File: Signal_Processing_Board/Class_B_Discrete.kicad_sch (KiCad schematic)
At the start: 29 parts, among them Q2 Q_amp-c-1, Q3 Q_amp-c-2, Q4 Q_amp-c-3, Q5 Q_amp-c-4, U11 U_amp-c_1, U12 U_amp-c_2

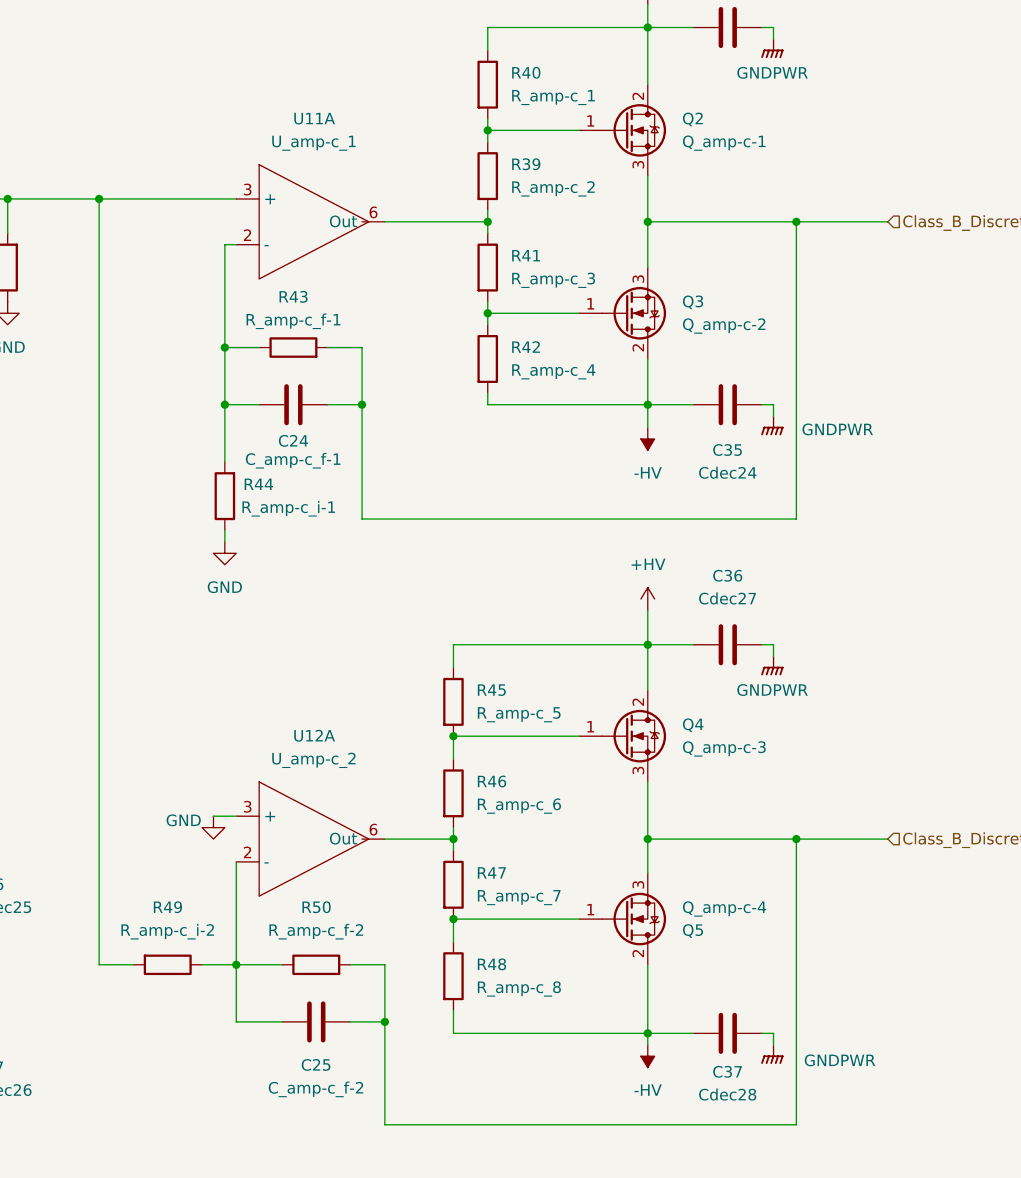
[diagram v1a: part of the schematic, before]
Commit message: First ordered version of Board
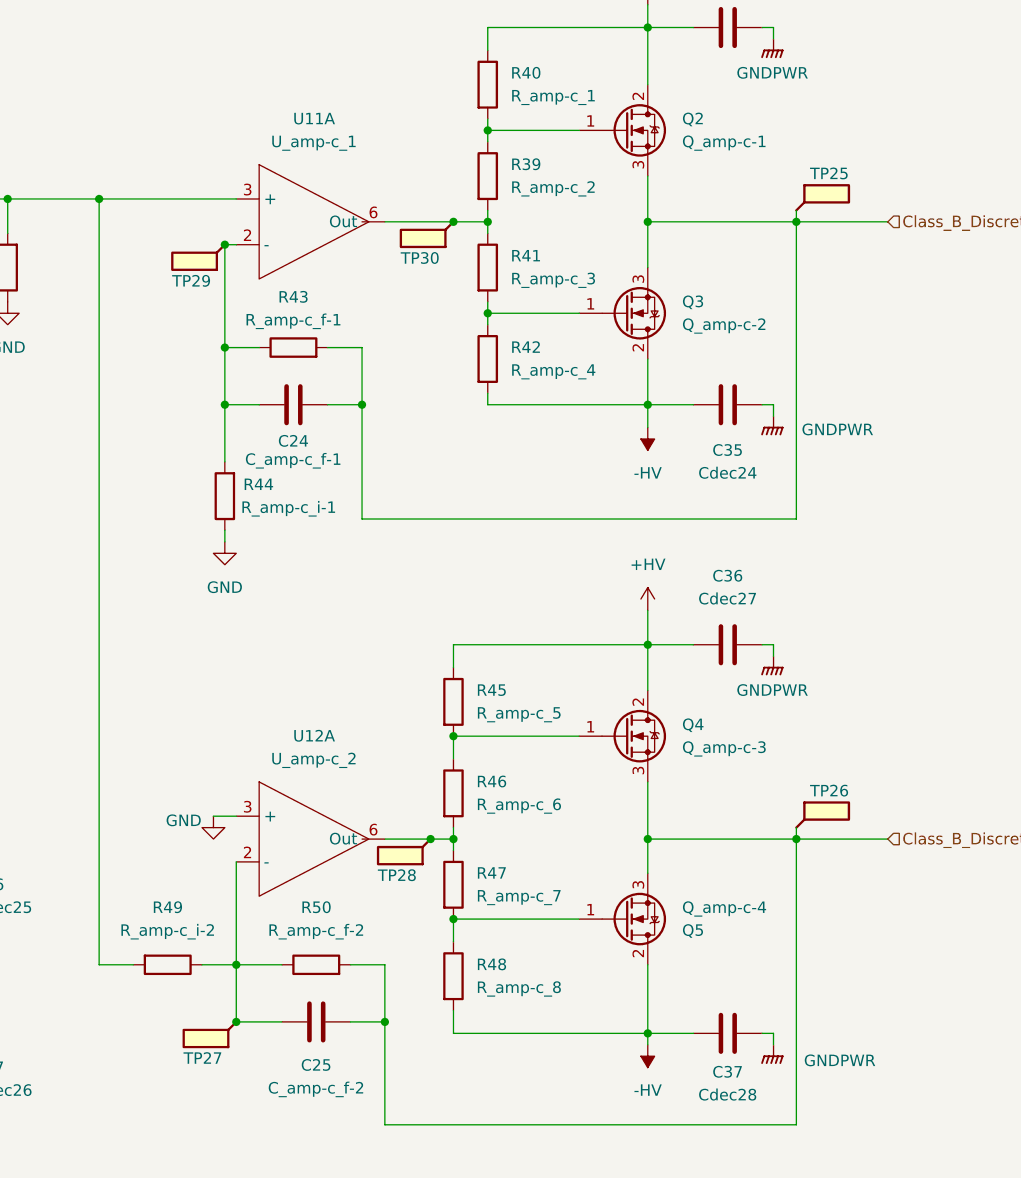
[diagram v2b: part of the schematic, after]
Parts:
- added TP25, TP26, TP27, TP28, TP29, TP30: TestPoint_Flag, TestPoint:TestPoint_Pad_D1.5mm, symbol Connector:TestPoint_Flag
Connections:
- net Class_B_Discrete_Out_+: now also TP25.1
- net Class_B_Discrete_Out_-: now also TP26.1
- net at R39.2, R41.1, U11.6 (Out): now also TP30.1
- net at C25.1, R49.1, R50.1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: now also TP27.1
- net at C24.1, R43.1, R44.2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: now also TP29.1
- net at R46.2, R47.1, U12.6 (Out): now also TP28.1

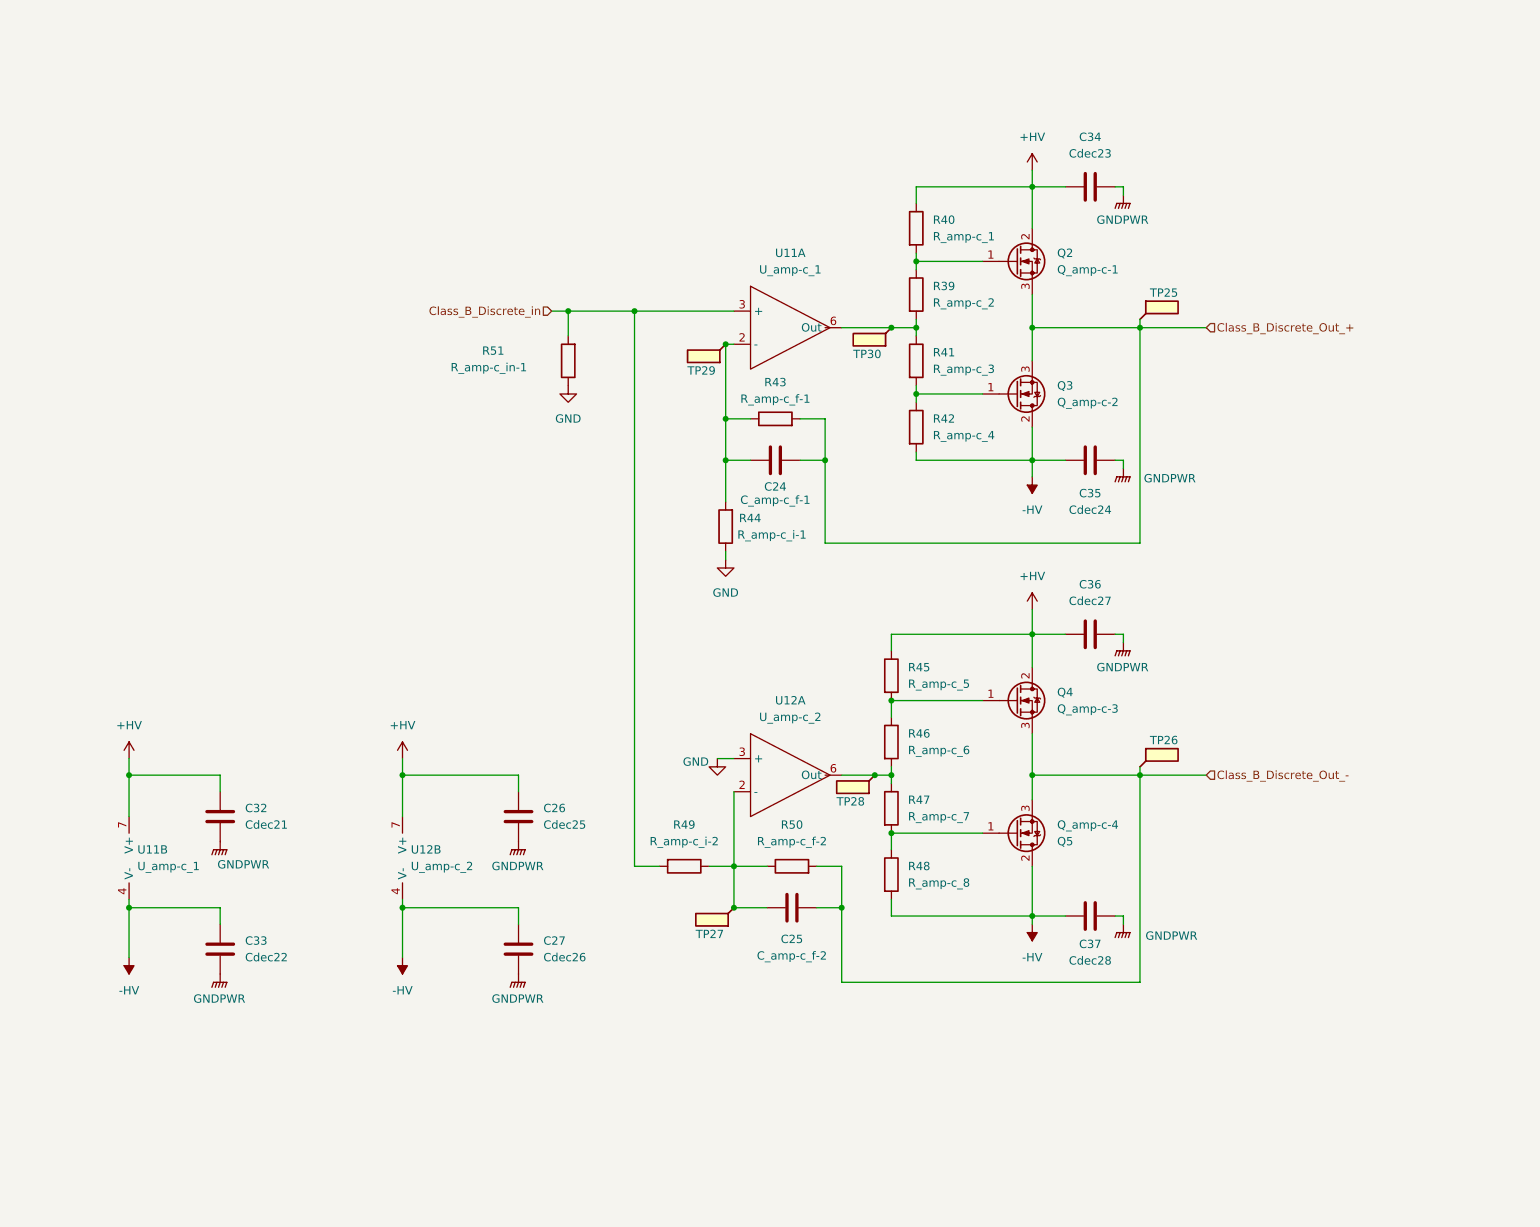
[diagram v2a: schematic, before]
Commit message: Final version of the board, updated with lessons from first version
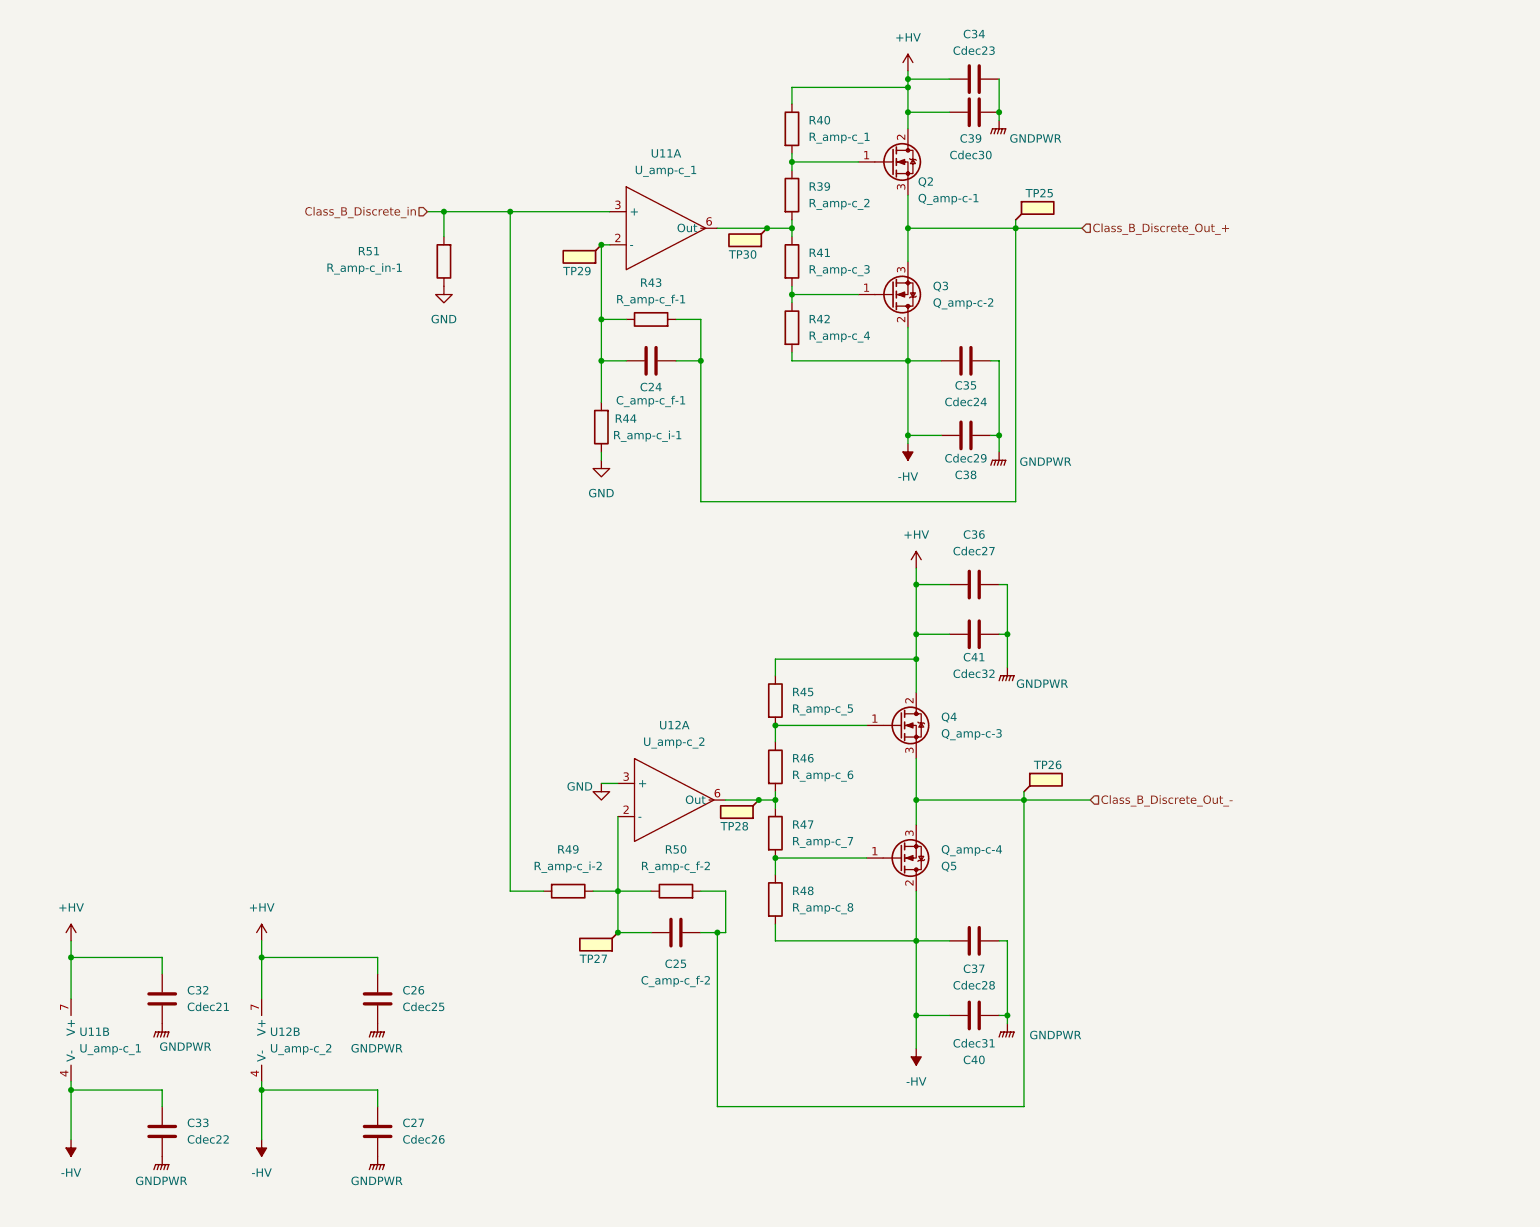
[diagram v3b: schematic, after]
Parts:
- added C38: Cdec29, Capacitor_THT:CP_Radial_D10.0mm_P5.00mm, symbol Device:C
- added C39: Cdec30, Capacitor_THT:CP_Radial_D10.0mm_P5.00mm, symbol Device:C
- added C40: Cdec31, Capacitor_THT:CP_Radial_D10.0mm_P5.00mm, symbol Device:C
- added C41: Cdec32, Capacitor_THT:CP_Radial_D10.0mm_P5.00mm, symbol Device:C
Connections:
- net +HV: now also C39.1, C41.1
- net -HV: now also C38.2, C40.2
- net GNDPWR: now also C38.1, C39.2, C40.1, C41.2
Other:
- moved on the sheet: C24, C25, C26, C27, C32, C33, C34, C35, C36, C37, Q2, Q3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

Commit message: Updated file structure and added PDF of schematic
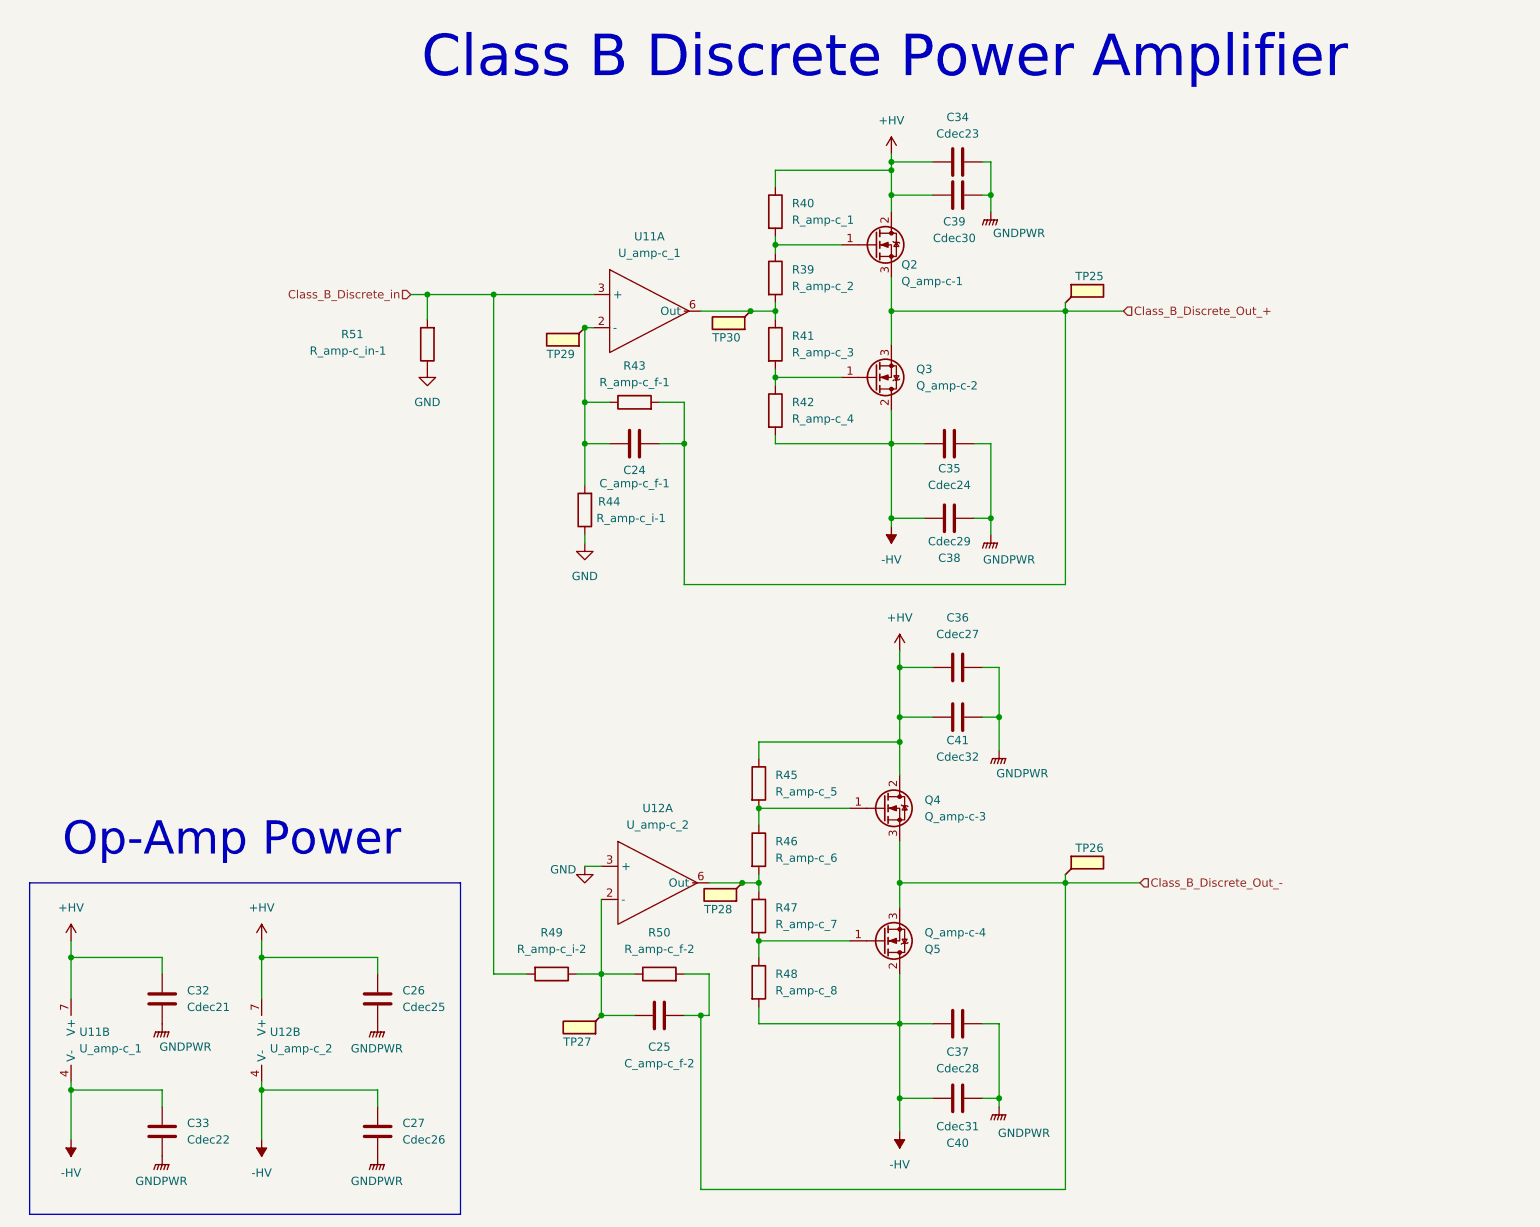
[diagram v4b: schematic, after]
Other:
- note added: "Class B Discrete Power Amplifier"
- note added: "Op-Amp Power"
- moved on the sheet: C24, C25, C34, C35, C36, C37, C38, C39, C40, C41, Q2, Q3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
